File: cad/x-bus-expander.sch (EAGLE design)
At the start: 56 parts, among them IC1 MCP23017SO, IC2 MCP23017SO

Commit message: Fixed a pcb bug when Arduion nano v2/v3 have different I2C pins placement.
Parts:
- R1: value (none) -> 10k
- RN1, RN2: value (none) -> 8x1k
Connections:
- net NANO_SCL: now also U$1.A2
- net NANO_SDA: now also U$1.A3
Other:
- note added: "8 x 2N7002"
- note added: "Dual footprint PTH/SMD RESISTOR"
- note added: "V2/V3 fix"
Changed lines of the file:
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@@
 <part name="IC2" library="adafruit" deviceset="MCP23017" device="SO"/>
 <part name="IN1" library="con-harting-ml" deviceset="ML16" device=""/>
-<part name="RN1" library="resistor-sil" deviceset="G08R" device=""/>
+<part name="RN1" library="resistor-sil" deviceset="G08R" device="" value="8x1k"/>
 <part name="C1" library="rcl" deviceset="C-US" device="C0805" value="220n"/>
 <part name="C2" library="rcl" deviceset="C-US" device="C0805" value="220n"/>
@@
 <part name="GND3" library="supply1" deviceset="GND" device=""/>
 <part name="P+4" library="supply1" deviceset="VCC" device=""/>
-<part name="R1" library="rcl" deviceset="R-US_" device="R0603"/>
+<part name="R1" library="rcl" deviceset="R-US_" device="R0603" value="10k"/>
 <part name="ADR" library="switch-dil" deviceset="DIP02YL" device=""/>
 <part name="R2" library="rcl" deviceset="R-US_" device="R0603" value="10k"/>
@@
 <part name="IC1" library="adafruit" deviceset="MCP23017" device="SO"/>
 <part name="IN2" library="con-harting-ml" deviceset="ML16" device=""/>
-<part name="RN2" library="resistor-sil" deviceset="G08R" device=""/>
+<part name="RN2" library="resistor-sil" deviceset="G08R" device="" value="8x1k"/>
 <part name="C10" library="rcl" deviceset="C-US" device="C0805" value="220n"/>
 <part name="C11" library="rcl" deviceset="C-US" device="C0805" value="220n"/>
@@
 <sheet>
 <plain>
+<text x="-154.94" y="-200.66" size="1.778" layer="97">Dual footprint PTH/SMD RESISTOR</text>
+<text x="-119.38" y="-139.7" size="1.778" layer="97">8 x 2N7002</text>
+<text x="25.4" y="-142.24" size="1.778" layer="97">8 x 2N7002</text>
+<text x="-195.58" y="-215.9" size="1.778" layer="97">V2/V3 fix</text>
 </plain>
 <instances>
@@
 <instance part="P+12" gate="VCC" x="-30.48" y="-78.74"/>
 <instance part="R4" gate="G$1" x="-30.48" y="-86.36" rot="R90"/>
-<instance part="U$1" gate="G$1" x="-213.36" y="-185.42"/>
+<instance part="U$1" gate="G$1" x="-223.52" y="-185.42"/>
 <instance part="IO" gate="G$1" x="-111.76" y="-223.52" rot="R180"/>
 <instance part="VIN" gate="-1" x="-226.06" y="-165.1" rot="R180"/>
@@
 <segment>
 <pinref part="U$1" gate="G$1" pin="A4"/>
-<wire x1="-187.96" y1="-228.6" x2="-167.64" y2="-228.6" width="0.1524" layer="91"/>
+<wire x1="-198.12" y1="-228.6" x2="-195.58" y2="-228.6" width="0.1524" layer="91"/>
 <label x="-182.88" y="-228.6" size="1.778" layer="95"/>
 <pinref part="IO" gate="G$1" pin="3"/>
+<wire x1="-195.58" y1="-228.6" x2="-167.64" y2="-228.6" width="0.1524" layer="91"/>
 <wire x1="-119.38" y1="-223.52" x2="-142.24" y2="-223.52" width="0.1524" layer="91"/>
 <wire x1="-142.24" y1="-223.52" x2="-147.32" y2="-223.52" width="0.1524" layer="91"/>
@@
 <pinref part="R7" gate="G$1" pin="1"/>
 <wire x1="-142.24" y1="-215.9" x2="-142.24" y2="-223.52" width="0.1524" layer="91"/>
+<junction x="-142.24" y="-223.52"/>
+<pinref part="U$1" gate="G$1" pin="A3"/>
+<wire x1="-198.12" y1="-223.52" x2="-195.58" y2="-223.52" width="0.1524" layer="91"/>
+<wire x1="-195.58" y1="-223.52" x2="-195.58" y2="-228.6" width="0.1524" layer="91"/>
+<junction x="-195.58" y="-228.6"/>
 </segment>
 </net>
@@
 <segment>
 <pinref part="U$1" gate="G$1" pin="A5"/>
-<wire x1="-187.96" y1="-233.68" x2="-165.1" y2="-233.68" width="0.1524" layer="91"/>
+<wire x1="-198.12" y1="-233.68" x2="-193.04" y2="-233.68" width="0.1524" layer="91"/>
 <label x="-182.88" y="-233.68" size="1.778" layer="95"/>
 <pinref part="IO" gate="G$1" pin="4"/>
+<wire x1="-193.04" y1="-233.68" x2="-165.1" y2="-233.68" width="0.1524" layer="91"/>
 <wire x1="-119.38" y1="-226.06" x2="-121.92" y2="-226.06" width="0.1524" layer="91"/>
 <wire x1="-121.92" y1="-226.06" x2="-127" y2="-226.06" width="0.1524" layer="91"/>
@@
 <pinref part="R8" gate="G$1" pin="1"/>
 <wire x1="-121.92" y1="-215.9" x2="-121.92" y2="-226.06" width="0.1524" layer="91"/>
+<junction x="-121.92" y="-226.06"/>
+<pinref part="U$1" gate="G$1" pin="A2"/>
+<wire x1="-198.12" y1="-218.44" x2="-193.04" y2="-218.44" width="0.1524" layer="91"/>
+<wire x1="-193.04" y1="-218.44" x2="-193.04" y2="-233.68" width="0.1524" layer="91"/>
+<junction x="-193.04" y="-233.68"/>
 </segment>
 </net>
@@
 <segment>
 <pinref part="U$1" gate="G$1" pin="D2"/>
-<wire x1="-218.44" y1="-208.28" x2="-223.52" y2="-208.28" width="0.1524" layer="91"/>
-<wire x1="-223.52" y1="-208.28" x2="-223.52" y2="-182.88" width="0.1524" layer="91"/>
-<wire x1="-223.52" y1="-182.88" x2="-160.02" y2="-182.88" width="0.1524" layer="91"/>
+<wire x1="-228.6" y1="-208.28" x2="-233.68" y2="-208.28" width="0.1524" layer="91"/>
+<wire x1="-233.68" y1="-208.28" x2="-233.68" y2="-182.88" width="0.1524" layer="91"/>
+<wire x1="-233.68" y1="-182.88" x2="-160.02" y2="-182.88" width="0.1524" layer="91"/>
 <wire x1="-160.02" y1="-182.88" x2="-160.02" y2="-228.6" width="0.1524" layer="91"/>
 <pinref part="IO" gate="G$1" pin="5"/>
@@
 <wire x1="-119.38" y1="-231.14" x2="-152.4" y2="-231.14" width="0.1524" layer="91"/>
 <pinref part="U$1" gate="G$1" pin="GND1"/>
-<wire x1="-187.96" y1="-193.04" x2="-162.56" y2="-193.04" width="0.1524" layer="91"/>
+<wire x1="-198.12" y1="-193.04" x2="-162.56" y2="-193.04" width="0.1524" layer="91"/>
 <wire x1="-162.56" y1="-193.04" x2="-162.56" y2="-231.14" width="0.1524" layer="91"/>
 <wire x1="-162.56" y1="-231.14" x2="-152.4" y2="-231.14" width="0.1524" layer="91"/>
@@
 <segment>
 <pinref part="U$1" gate="G$1" pin="+5V"/>
-<wire x1="-187.96" y1="-203.2" x2="-157.48" y2="-203.2" width="0.1524" layer="91"/>
+<wire x1="-198.12" y1="-203.2" x2="-157.48" y2="-203.2" width="0.1524" layer="91"/>
 <wire x1="-157.48" y1="-203.2" x2="-157.48" y2="-220.98" width="0.1524" layer="91"/>
 <pinref part="IO" gate="G$1" pin="2"/>

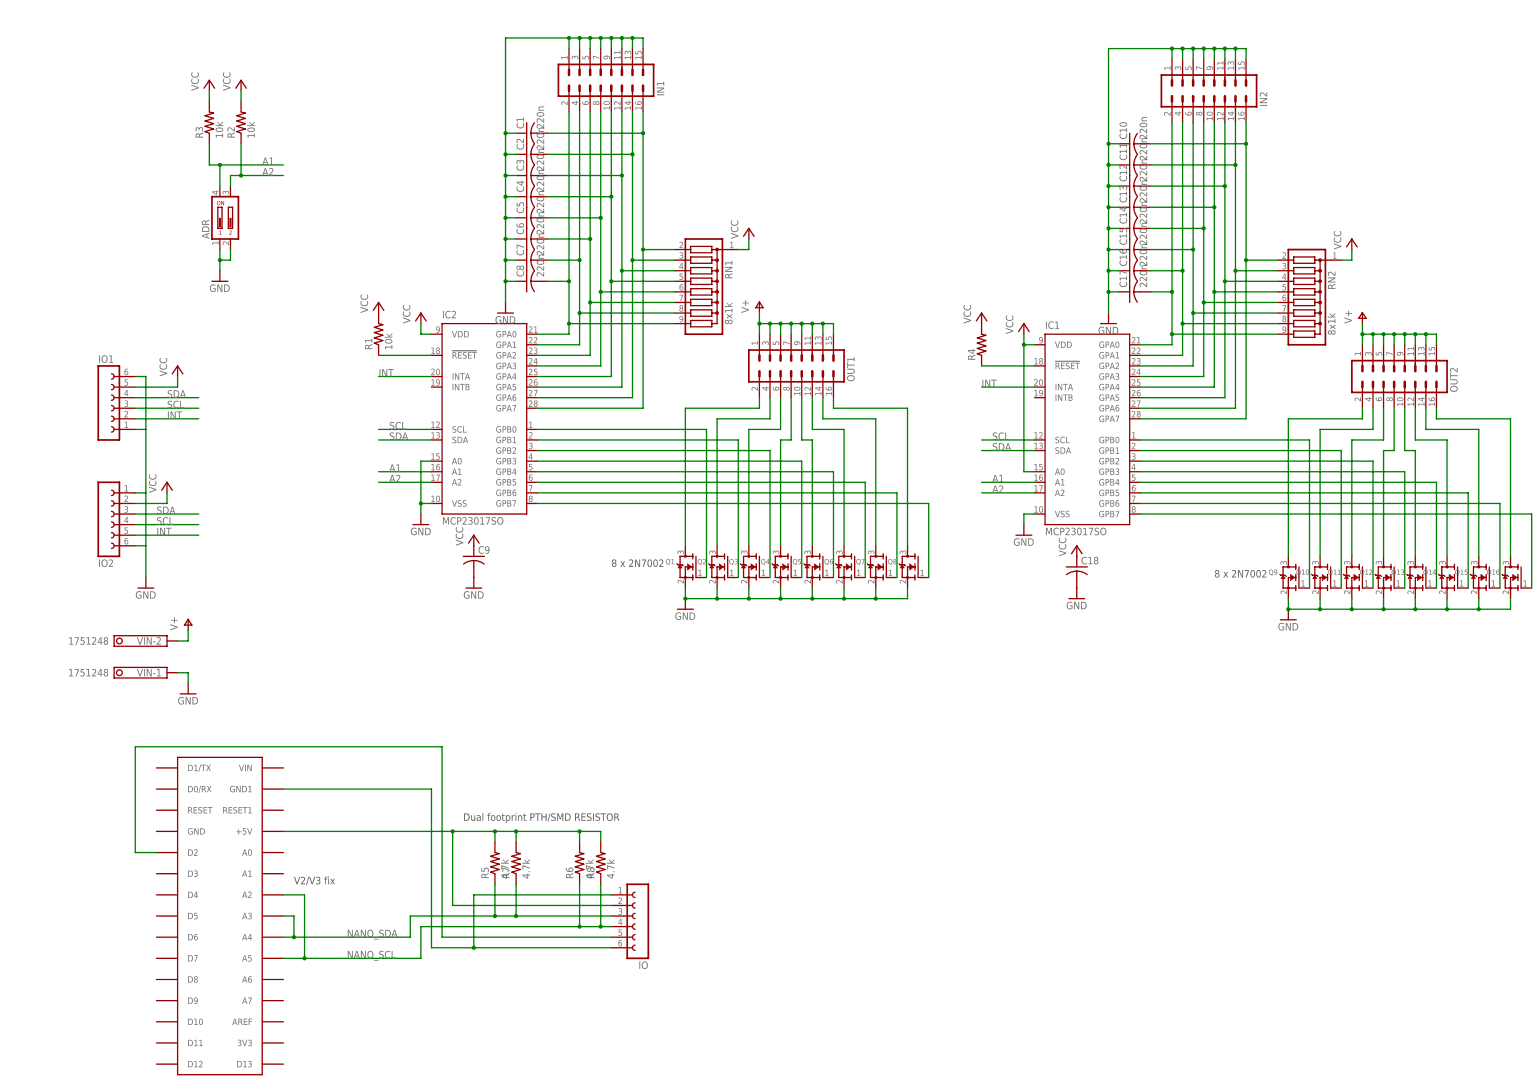
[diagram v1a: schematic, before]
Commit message: Updated schematic with some information and generated pdf for schematic.
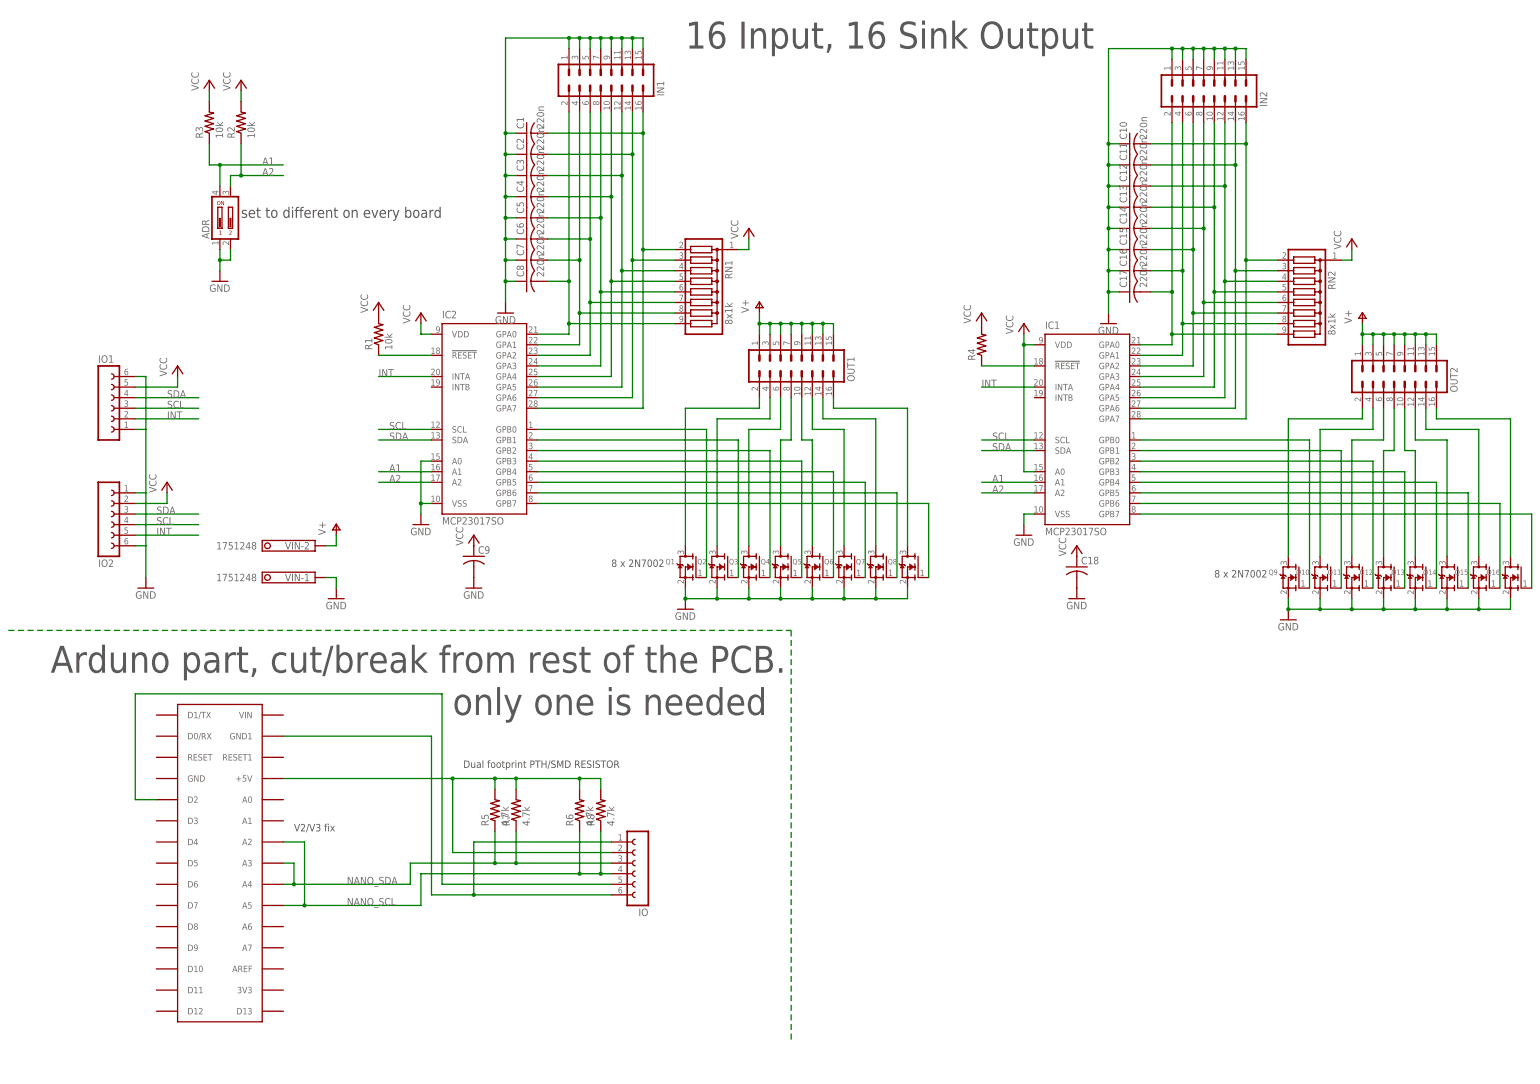
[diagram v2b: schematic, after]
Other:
- note added: "16 Input, 16 Sink Output"
- note added: "Arduno part, cut/break from rest of the PCB."
- note added: "only one is needed"
- note added: "set to different on every board"
- moved on the sheet: IO, R5, R6, R7, R8, VIN-1, VIN-2
